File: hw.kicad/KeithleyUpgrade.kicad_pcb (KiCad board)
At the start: 2 copper layers, 190.1 x 75.6 mm, 73 parts, among them J1 DEBUG_PORT, J14 DISPLAY_BOARD, K1 TRIGGER, P1 PROG, P18 CONN_8, P8 TP1, P9 TP1, Q1 BC850, U1 24AA256, U2 FT230x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

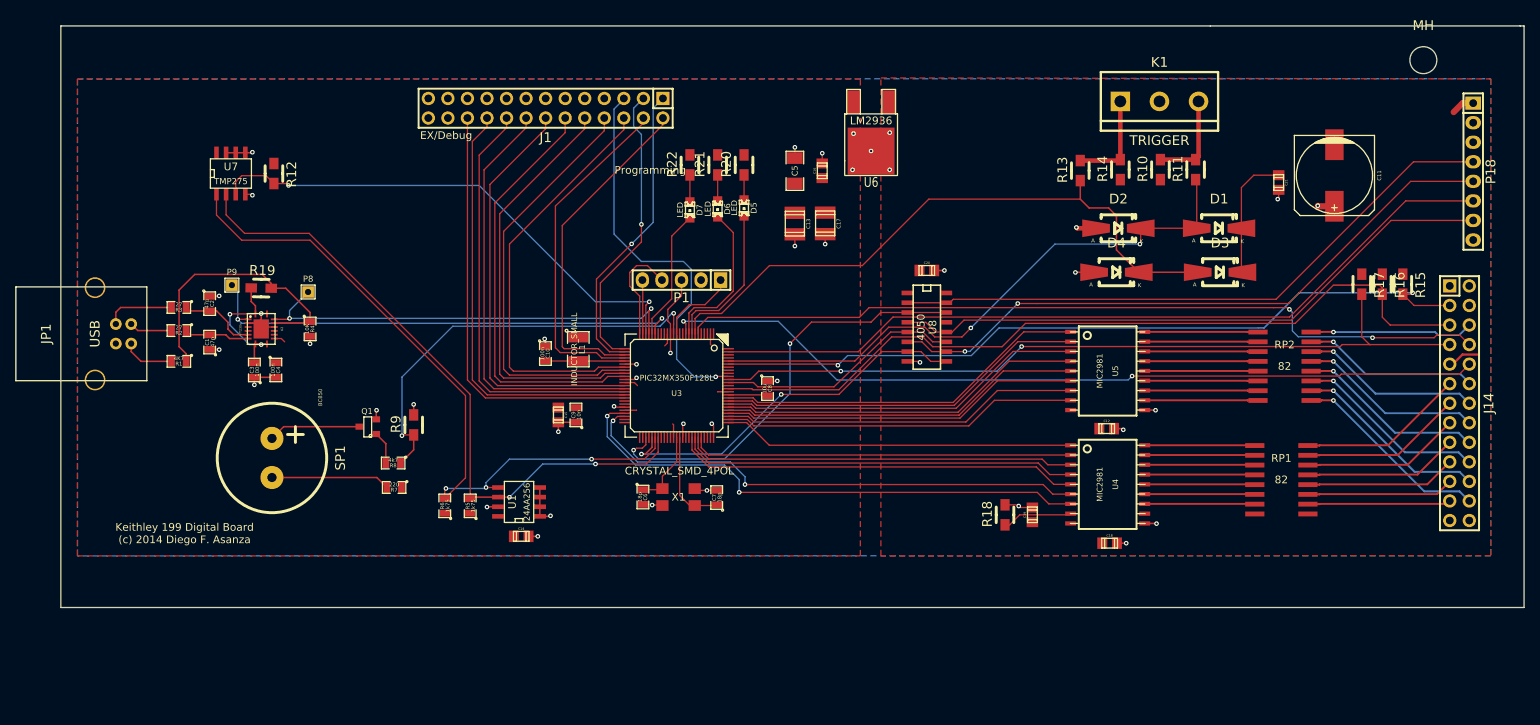
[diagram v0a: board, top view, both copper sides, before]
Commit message: fixed cristal footprint
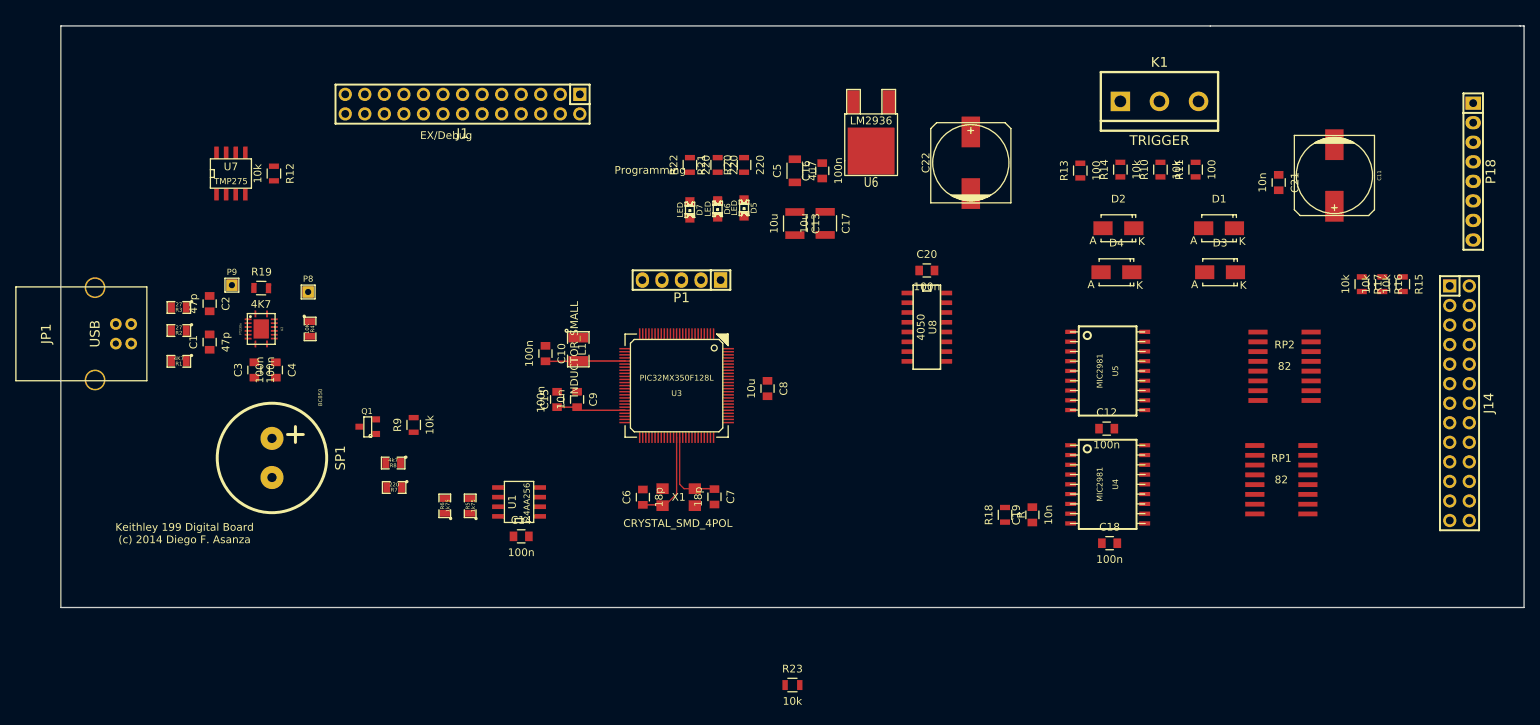
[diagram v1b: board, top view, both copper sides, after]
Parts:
- removed MH: MountingHole_3-5mm_RevA_Date21Jun2010, Mounting_Holes:MountingHole_3-5mm
- added C22: 220u/10v, Capacitors_SMD:c_elec_10x10, F.Cu at (168.9, 76.2)
- added R23: 10k, Resistors_SMD:R_0805, F.Cu at (145.7, 144.1)
- C1, C10, C2, C3, C4, C6, C7, C8, C9: footprint SMD_Packages:SM0805 -> Capacitors_SMD:C_0805
- C12, C14, C15, C16, C18, C19, C20, C21: footprint Capacitors_SMD:c_0805 -> Capacitors_SMD:C_0805
- C13, C17: footprint Capacitors_SMD:c_1210 -> Capacitors_SMD:C_1210
- C5: footprint SMD_Packages:SM1206 -> Capacitors_SMD:C_1206
- D1, D2, D3, D4: footprint Diodes_SMD:Diode-Universal-SMA-SMB_Handsoldering -> Diodes_SMD:Diode-SMA_Standard
- L1: footprint SMD_Packages:SM1210 -> SMD_Packages:SMD-1210
- R10, R11, R12, R13, R14, R15, R16, R17, R18, R19, R20, R21, R22, R9: footprint Resistors_SMD:Resistor_SMD0805_HandSoldering -> Resistors_SMD:R_0805
- moved J1 10.8 mm to (102.9, 68.6)
- moved C15 2.02 mm to (115.2, 107.0)
- moved C9 2.02 mm to (117.8, 107.0), turned to 270 degrees
- moved C7 0.31 mm to (135.6, 119.6), turned to 270 degrees
- turned X1 to 180 degrees
- turned C6 to 90 degrees
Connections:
- net +5V renamed VCC
- X1 pad 1: Net-(C6-Pad1) -> GND
- X1 pad 2: Net-(C7-Pad1) -> GND
- X1 pad 3: GND -> Net-(C6-Pad1)
- X1 pad 4: GND -> Net-(C7-Pad1)
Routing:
- net GND: track 113.5 -> 0.00 mm, vias 43 -> 0
- net /~CLOCK: track 107.9 -> 0.00 mm, vias 2 -> 0
- net /DATA: track 106.0 -> 0.00 mm, vias 2 -> 0
- net /S1: track 105.1 -> 0.00 mm
- net /ACOUNT: track 104.9 -> 0.00 mm
- net /S0: track 102.9 -> 0.00 mm, vias 2 -> 0
- net /S2: track 102.0 -> 0.00 mm, vias 2 -> 0
- net /SDA: track 93.4 -> 0.00 mm, vias 3 -> 0
- net /SCL: track 86.8 -> 0.00 mm, vias 2 -> 0
- net Net-(P18-Pad5): track 83.3 -> 0.00 mm, vias 2 -> 0
- net /EXTTRG: track 82.7 -> 0.00 mm
- net Net-(P18-Pad4): track 81.1 -> 0.00 mm
- net Net-(P18-Pad7): track 80.5 -> 0.00 mm
- net /VCOMP: track 76.6 -> 0.00 mm, vias 2 -> 0
- net /d1: track 69.9 -> 0.00 mm, vias 2 -> 0
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- removed copper zone on F.Cu, net +3.3V
- removed copper zone on B.Cu, net GND
- removed copper zone on F.Cu, net VCC

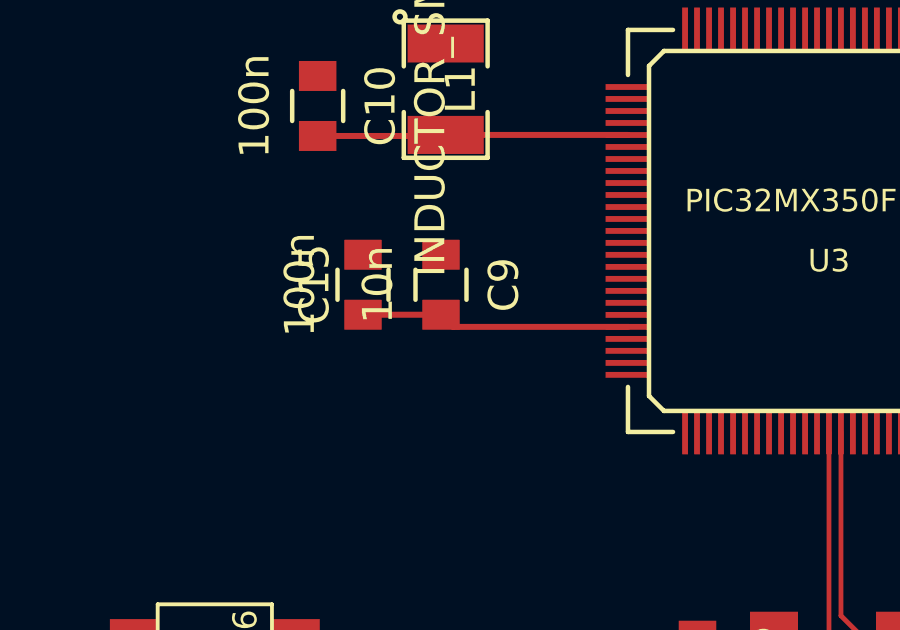
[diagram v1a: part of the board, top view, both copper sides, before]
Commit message: integrate scpi. implement idn command
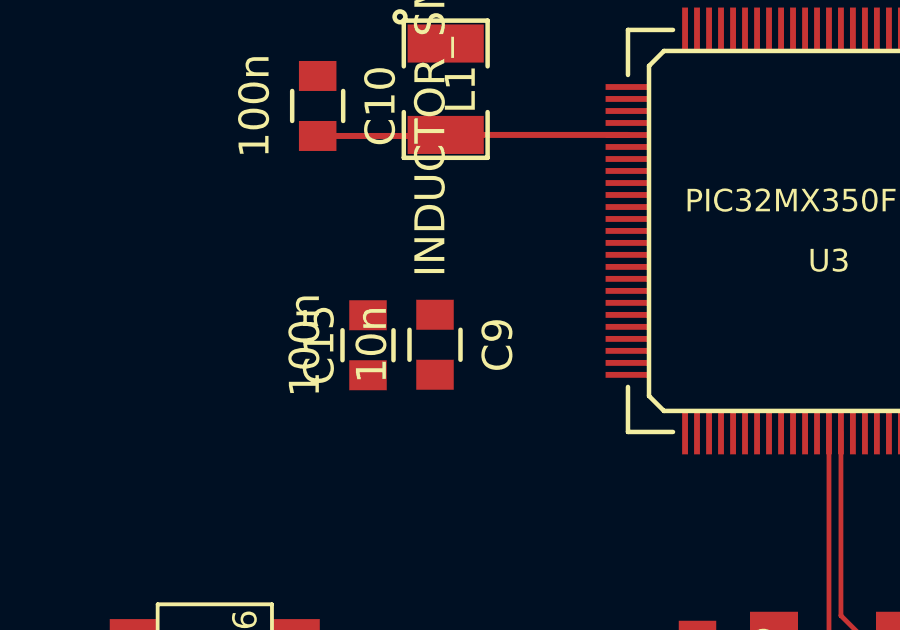
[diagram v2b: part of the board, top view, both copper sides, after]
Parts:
- moved C15 2.02 mm to (115.3, 109.0)
- moved C9 2.01 mm to (117.5, 109.0)
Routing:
- net +3.3V: track 9.00 -> 0.00 mm
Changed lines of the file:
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@@
     (thickness 1.6)
     (drawings 23)
-    (tracks 17)
+    (tracks 14)
     (zones 0)
     (modules 74)
@@
   )
   (module Capacitors_SMD:C_0805 (layer F.Cu)
-    (at 117.75 106.95 270)
+    (at 117.55 108.95 270)
     (descr "Capacitor SMD 0805, reflow soldering, AVX (see smccp.pdf)")
     (tags "capacitor 0805")
@@
   )
   (module Capacitors_SMD:C_0805 (layer F.Cu)
-    (at 115.15 106.95 270)
+    (at 115.316 108.966 270)
     (descr "Capacitor SMD 0805, reflow soldering, AVX (see smccp.pdf)")
     (tags "capacitor 0805")
@@
   (gr_line (start 50.673 133.985) (end 200.025 133.985) (angle 90) (layer Edge.Cuts) (width 0.15))
   (gr_line (start 50.673 58.42) (end 50.673 133.985) (angle 90) (layer Edge.Cuts) (width 0.15))
-  (segment (start 117.75 107.95) (end 115.15 107.95) (width 0.2) (layer F.Cu) (net 1))
-  (segment (start 123.98502 108.35386) (end 118.15386 108.35386) (width 0.2) (layer F.Cu) (net 1))
-  (segment (start 118.15386 108.35386) (end 117.75 107.95) (width 0.2) (layer F.Cu) (net 1))
   (segment (start 126.3 120.65) (end 128.75 120.65) (width 0.2) (layer F.Cu) (net 68) (status C00000))
   (segment (start 128.75 120.65) (end 128.85 120.75) (width 0.2) (layer F.Cu) (net 68) (status C00000))
